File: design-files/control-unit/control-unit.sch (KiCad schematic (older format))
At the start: 126 parts, among them SW501 SW_Push, U501 74HCT04, U502 74HCT161, U503 AT28C64, U504 AT28C64, U505 74HCT273, U506 74HCT377, U507 4002, U508 74HCT32, U509 AT28C64, U510 74HCT08, U511 74HCT157, U512 AT28C64, U513 74HCT173, U514 74HCT173, U515 74HCT08

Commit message: control-unit: Add a .1 second RC delay on the reset button so that _RST is asserted momentarily at power-up.
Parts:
- added C?: 1µF, symbol Device:CP1_Small
- R501: value 1K -> 100K
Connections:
- net GND: now also C?.2
- net ~RST: now also C?.1
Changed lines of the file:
@@
 P 700 5200
 F 0 "R501" H 759 5246 50  0000 L CNN
-F 1 "1K" H 759 5155 50  0000 L CNN
+F 1 "100K" H 759 5155 50  0000 L CNN
 F 2 "Resistor_THT:R_Axial_DIN0204_L3.6mm_D1.6mm_P5.08mm_Horizontal" H 700 5200 50  0001 C CNN
 F 3 "~" H 700 5200 50  0001 C CNN
@@
 	700  5300 700  5400
 Wire Wire Line
-	950  5400 700  5400
+	950  5400 900  5400
 Connection ~ 700  5400
 Wire Wire Line
@@
 Connection ~ 10100 5450
 Connection ~ 9550 5450
+$Comp
+L Device:CP1_Small C?
+U 1 1 63D116B5
+P 900 5550
+F 0 "C?" H 991 5596 50  0000 L CNN
+F 1 "1µF" H 991 5505 50  0000 L CNN
+F 2 "" H 900 5550 50  0001 C CNN
+F 3 "~" H 900 5550 50  0001 C CNN
+	1    900  5550
+	1    0    0    -1
+$EndComp
+Connection ~ 900  5400
+Wire Wire Line
+	900  5400 700  5400
+$Comp
+L power:GND #PWR?
+U 1 1 63D1374A
+P 900 5650
+F 0 "#PWR?" H 900 5400 50  0001 C CNN
+F 1 "GND" H 905 5477 50  0000 C CNN
+F 2 "" H 900 5650 50  0001 C CNN
+F 3 "" H 900 5650 50  0001 C CNN
+	1    900  5650
+	1    0    0    -1
+$EndComp
+Wire Wire Line
+	900  5450 900  5400
 $EndSCHEMATC

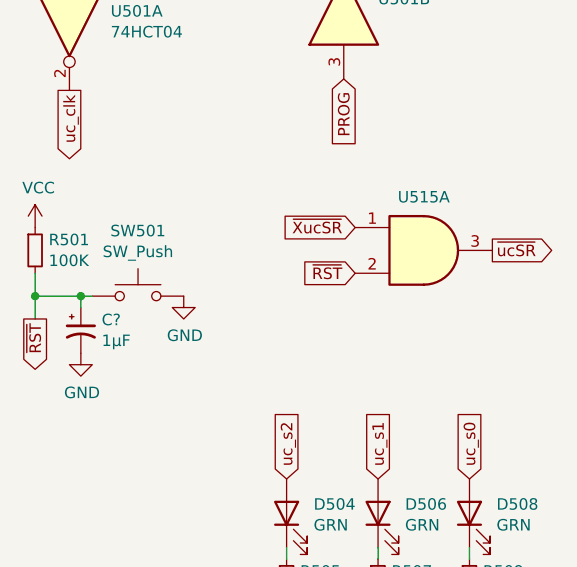
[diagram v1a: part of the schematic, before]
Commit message: control-unit: Discharge the capacitor on the reset signal through a 1K resistor.
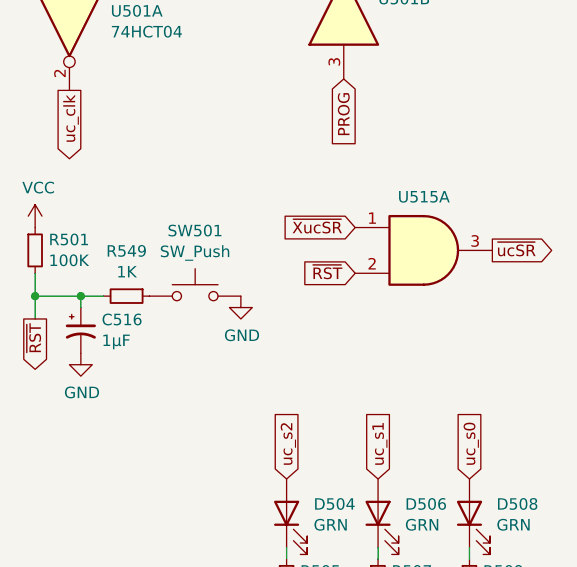
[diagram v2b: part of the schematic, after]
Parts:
- added R549: 1K, symbol Device:R_Small
- C516: renamed from C?; footprint (none) -> Capacitor_THT:CP_Radial_D6.3mm_P2.50mm; Mouser (none) -> 647-UVY2D010MED1TA
- R501: Mouser 594-SFR16S0001001JR5 -> 594-SFR16S0001003JA5
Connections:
- net ~RST: now also R549.2; no longer SW501.1
- new net: R549.1, SW501.1
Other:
- moved on the sheet: SW501
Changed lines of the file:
@@
 L Switch:SW_Push SW501
 U 1 1 630BB0DA
-P 1150 5400
-F 0 "SW501" H 1150 5685 50  0000 C CNN
-F 1 "SW_Push" H 1150 5594 50  0000 C CNN
-F 2 "Button_Switch_THT:SW_TH_Tactile_Omron_B3F-10xx" H 1150 5600 50  0001 C CNN
-F 3 "~" H 1150 5600 50  0001 C CNN
-F 4 "179-TS0266150BK100SC" H 1150 5400 50  0001 C CNN "Mouser"
-	1    1150 5400
+P 1400 5400
+F 0 "SW501" H 1400 5685 50  0000 C CNN
+F 1 "SW_Push" H 1400 5594 50  0000 C CNN
+F 2 "Button_Switch_THT:SW_TH_Tactile_Omron_B3F-10xx" H 1400 5600 50  0001 C CNN
+F 3 "~" H 1400 5600 50  0001 C CNN
+F 4 "179-TS0266150BK100SC" H 1400 5400 50  0001 C CNN "Mouser"
+	1    1400 5400
 	1    0    0    -1
 $EndComp
@@
 F 2 "Resistor_THT:R_Axial_DIN0204_L3.6mm_D1.6mm_P5.08mm_Horizontal" H 700 5200 50  0001 C CNN
 F 3 "~" H 700 5200 50  0001 C CNN
-F 4 "594-SFR16S0001001JR5" H 700 5200 50  0001 C CNN "Mouser"
+F 4 "594-SFR16S0001003JA5" H 700 5200 50  0001 C CNN "Mouser"
 	1    700  5200
 	1    0    0    -1
@@
 Wire Wire Line
 	700  5300 700  5400
-Wire Wire Line
-	950  5400 900  5400
 Connection ~ 700  5400
 Wire Wire Line
@@
 L power:GND #PWR0159
 U 1 1 6310BDAF
-P 1350 5400
-F 0 "#PWR0159" H 1350 5150 50  0001 C CNN
-F 1 "GND" H 1355 5227 50  0000 C CNN
-F 2 "" H 1350 5400 50  0001 C CNN
-F 3 "" H 1350 5400 50  0001 C CNN
-	1    1350 5400
+P 1600 5400
+F 0 "#PWR0159" H 1600 5150 50  0001 C CNN
+F 1 "GND" H 1605 5227 50  0000 C CNN
+F 2 "" H 1600 5400 50  0001 C CNN
+F 3 "" H 1600 5400 50  0001 C CNN
+	1    1600 5400
 	1    0    0    -1
 $EndComp
@@
 Connection ~ 9550 5450
 $Comp
-L Device:CP1_Small C?
+L Device:CP1_Small C516
 U 1 1 63D116B5
 P 900 5550
-F 0 "C?" H 991 5596 50  0000 L CNN
+F 0 "C516" H 991 5596 50  0000 L CNN
 F 1 "1µF" H 991 5505 50  0000 L CNN
-F 2 "" H 900 5550 50  0001 C CNN
+F 2 "Capacitor_THT:CP_Radial_D6.3mm_P2.50mm" H 900 5550 50  0001 C CNN
 F 3 "~" H 900 5550 50  0001 C CNN
+F 4 "647-UVY2D010MED1TA" H 900 5550 50  0001 C CNN "Mouser"
 	1    900  5550
 	1    0    0    -1
@@
 	900  5400 700  5400
 $Comp
-L power:GND #PWR?
+L power:GND #PWR0209
 U 1 1 63D1374A
 P 900 5650
-F 0 "#PWR?" H 900 5400 50  0001 C CNN
+F 0 "#PWR0209" H 900 5400 50  0001 C CNN
 F 1 "GND" H 905 5477 50  0000 C CNN
 F 2 "" H 900 5650 50  0001 C CNN
@@
 Wire Wire Line
 	900  5450 900  5400
+$Comp
+L Device:R_Small R549
+U 1 1 63D3F3F9
+P 1100 5400
+F 0 "R549" V 904 5400 50  0000 C CNN
+F 1 "1K" V 995 5400 50  0000 C CNN
+F 2 "" H 1100 5400 50  0001 C CNN
+F 3 "~" H 1100 5400 50  0001 C CNN
+F 4 "594-SFR16S0001001JR5" V 1100 5400 50  0001 C CNN "Mouser"
+	1    1100 5400
+	0    1    1    0
+$EndComp
+Wire Wire Line
+	900  5400 1000 5400
 $EndSCHEMATC

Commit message: Connect the insn latch, CC latch, and CC register to _RST.
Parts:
- R549: footprint (none) -> Resistor_THT:R_Axial_DIN0204_L3.6mm_D1.6mm_P5.08mm_Horizontal
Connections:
- net GND: no longer U513.15 (Mr)
- net VCC: no longer U505.1 (~Mr)
- net ~RST: now also U505.1 (~Mr)
- net cc_rst: now reaches U501.8, U514.15 (Mr)
- net cc_rst: now also U513.15 (Mr)
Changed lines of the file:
@@
 uc_clk
 $Comp
-L power:VCC #PWR0114
-U 1 1 6222178D
-P 5100 3750
-F 0 "#PWR0114" H 5100 3600 50  0001 C CNN
-F 1 "VCC" V 5115 3878 50  0000 L CNN
-F 2 "" H 5100 3750 50  0001 C CNN
-F 3 "" H 5100 3750 50  0001 C CNN
-	1    5100 3750
-	0    1    1    0
-$EndComp
-$Comp
 L power:GND #PWR0115
 U 1 1 62221D2F
@@
 $EndComp
 Connection ~ 9200 3950
-$Comp
-L power:GND #PWR0119
-U 1 1 629B2C28
-P 9200 4650
-F 0 "#PWR0119" H 9200 4400 50  0001 C CNN
-F 1 "GND" V 9205 4522 50  0000 R CNN
-F 2 "" H 9200 4650 50  0001 C CNN
-F 3 "" H 9200 4650 50  0001 C CNN
-	1    9200 4650
-	0    1    1    0
-$EndComp
 Text Notes 9650 4200 0    50   Italic 10
 CC\nLatch
@@
 F 0 "R549" V 904 5400 50  0000 C CNN
 F 1 "1K" V 995 5400 50  0000 C CNN
-F 2 "" H 1100 5400 50  0001 C CNN
+F 2 "Resistor_THT:R_Axial_DIN0204_L3.6mm_D1.6mm_P5.08mm_Horizontal" H 1100 5400 50  0001 C CNN
 F 3 "~" H 1100 5400 50  0001 C CNN
 F 4 "594-SFR16S0001001JR5" V 1100 5400 50  0001 C CNN "Mouser"
@@
 Wire Wire Line
 	900  5400 1000 5400
+Text GLabel 5100 3750 3    50   Input ~ 0
+~RST
+Text GLabel 15000 5200 3    50   Output ~ 0
+cc_rst
+Wire Wire Line
+	15000 5200 15000 4900
+Connection ~ 15000 4900
+Text GLabel 9200 4650 0    50   Input ~ 0
+cc_rst
 $EndSCHEMATC

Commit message: For ALU_B, don't use an AND gate with CLK to do the write-enable, as this could cause spurious rising-edges, and thus spurious loads into the register.  Use a pair of '157 muxes in front of the register intead. Change the ALB signal back to _ALB (active-low).
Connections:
- net GND: no longer R540.2
- net VCC: now also R540.2
- net at R540.1: now also D539.2 (A); no longer D539.1 (K)
- net ALB renamed ~ALB
- net ~ALB: now also D539.1 (K); no longer D539.2 (A)
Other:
- moved on the sheet: D539
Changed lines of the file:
@@
 ALS2
 Text GLabel 8850 900  1    50   Output ~ 0
-ALB
+~ALB
 Text GLabel 9000 900  1    50   Output ~ 0
 ~ALW
@@
 $EndComp
 $Comp
-L Device:LED D539
-U 1 1 6321D30E
-P 14550 7750
-F 0 "D539" V 14589 7632 50  0000 R CNN
-F 1 "GRN" V 14498 7632 50  0000 R CNN
-F 2 "LED_THT:LED_D5.0mm" H 14550 7750 50  0001 C CNN
-F 3 "~" H 14550 7750 50  0001 C CNN
-	1    14550 7750
-	0    -1   -1   0
-$EndComp
-$Comp
 L Device:R_Small R540
 U 1 1 6321D314
@@
 $EndComp
 $Comp
-L power:GND #PWR0176
-U 1 1 6321D32C
-P 14550 8150
-F 0 "#PWR0176" H 14550 7900 50  0001 C CNN
-F 1 "GND" H 14555 7977 50  0000 C CNN
-F 2 "" H 14550 8150 50  0001 C CNN
-F 3 "" H 14550 8150 50  0001 C CNN
-	1    14550 8150
-	1    0    0    -1
-$EndComp
-$Comp
 L power:GND #PWR0177
 U 1 1 6321D33E
@@
 ~ALW
 Text GLabel 14550 7600 1    50   Input ~ 0
-ALB
+~ALB
 $Comp
 L Device:LED D524
@@
 Text GLabel 9200 4650 0    50   Input ~ 0
 cc_rst
+$Comp
+L power:VCC #PWR?
+U 1 1 623040CC
+P 14550 8150
+F 0 "#PWR?" H 14550 8000 50  0001 C CNN
+F 1 "VCC" H 14565 8323 50  0000 C CNN
+F 2 "" H 14550 8150 50  0001 C CNN
+F 3 "" H 14550 8150 50  0001 C CNN
+	1    14550 8150
+	-1   0    0    1
+$EndComp
+$Comp
+L Device:LED D539
+U 1 1 6321D30E
+P 14550 7750
+F 0 "D539" V 14500 7650 50  0000 R CNN
+F 1 "GRN" V 14600 7650 50  0000 R CNN
+F 2 "LED_THT:LED_D5.0mm" H 14550 7750 50  0001 C CNN
+F 3 "~" H 14550 7750 50  0001 C CNN
+	1    14550 7750
+	0    -1   1    0
+$EndComp
 $EndSCHEMATC

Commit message: Rework to use DIP register packs for the LEDs.
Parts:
- removed R502, R503, R504, R505, R506, R507, R508, R509, R510, R511, R512, R513, R514, R515, R516, R517, R518, R519, R520, R521, R522, R523, R524, R525, R526, R527, R528, R529, R530, R531, R532, R533, R534, R535, R536, R537, R538, R539, R540, R541, R542, R543, R544, R545, R546, R547, R548: 330, Resistor_THT:R_Axial_DIN0204_L3.6mm_D1.6mm_P5.08mm_Horizontal, symbol Device:R_Small
- added D548: YEL, LED_THT:LED_D5.0mm, symbol Device:LED
- added RN501: 330x8, Package_DIP:DIP-16_W7.62mm_Socket, symbol Device:R_Pack08_Split
- added RN502, RN503, RN504, RN505, RN506: 330 x 8, Package_DIP:DIP-16_W7.62mm_Socket, symbol Device:R_Pack08
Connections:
- net GND: now also RN501.1 (R1.1), RN501.2 (R2.1), RN501.3 (R3.1), RN501.4 (R4.1), RN501.5 (R5.1), RN501.6 (R6.1), RN501.7 (R7.1), RN501.8 (R8.1), RN502.3 (R3.1), RN502.4 (R4.1), RN502.5 (R5.1), RN503.2 (R2.1), RN503.4 (R4.1), RN505.1 (R1.1), RN505.2 (R2.1), RN505.3 (R3.1), RN505.4 (R4.1), RN505.5 (R5.1), RN505.6 (R6.1), RN505.7 (R7.1), RN505.8 (R8.1), RN506.1 (R1.1), RN506.5 (R5.1), RN506.6 (R6.1), RN506.7 (R7.1), RN506.8 (R8.1)
- net VCC: now also RN502.1 (R1.1), RN502.2 (R2.1), RN502.6 (R6.1), RN502.7 (R7.1), RN502.8 (R8.1), RN503.1 (R1.1), RN503.3 (R3.1), RN503.5 (R5.1), RN503.6 (R6.1), RN503.7 (R7.1), RN503.8 (R8.1), RN504.1 (R1.1), RN504.2 (R2.1), RN504.3 (R3.1), RN504.4 (R4.1), RN504.5 (R5.1), RN504.6 (R6.1), RN504.7 (R7.1), RN504.8 (R8.1), RN506.2 (R2.1), RN506.3 (R3.1), RN506.4 (R4.1)
- net uc_clk: now also D548.2 (A)
- net at D540.1 (K): now also RN501.12 (R5.2)
- net at D542.1 (K): now also RN501.11 (R6.2)
- net at D544.1 (K): now also RN501.10 (R7.2)
- net at D546.1 (K): now also RN501.9 (R8.2)
- net at D532.1 (K): now also RN505.12 (R5.2)
- net at D533.1 (K): now also RN505.11 (R6.2)
- net at D535.1 (K): now also RN505.10 (R7.2)
- net at D537.1 (K): now also RN505.9 (R8.2)
- net at D525.1 (K): now also RN505.16 (R1.2)
- net at D527.1 (K): now also RN505.15 (R2.2)
- net at D529.1 (K): now also RN505.14 (R3.2)
- net at D531.1 (K): now also RN505.13 (R4.2)
- net at D541.1 (K): now also RN506.12 (R5.2)
- net at D543.1 (K): now also RN506.11 (R6.2)
- net at D545.1 (K): now also RN506.10 (R7.2)
- net at D547.1 (K): now also RN506.9 (R8.2)
- net at D534.1 (K): now also RN506.16 (R1.2)
- net at D536.2 (A): now also RN506.15 (R2.2)
- net at D538.2 (A): now also RN506.14 (R3.2)
- net at D539.2 (A): now also RN506.13 (R4.2)
- net at D524.2 (A): now also RN504.12 (R5.2)
- net at D526.2 (A): now also RN504.11 (R6.2)
- net at D528.2 (A): now also RN504.10 (R7.2)
- net at D530.2 (A): now also RN504.9 (R8.2)
- net at D520.2 (A): now also RN504.16 (R1.2)
- net at D521.2 (A): now also RN504.15 (R2.2)
- net at D522.2 (A): now also RN504.14 (R3.2)
- net at D523.2 (A): now also RN504.13 (R4.2)
- net at D516.2 (A): now also RN503.12 (R5.2)
- net at D517.2 (A): now also RN503.11 (R6.2)
- net at D518.2 (A): now also RN503.10 (R7.2)
- net at D519.2 (A): now also RN503.9 (R8.2)
- net at D512.2 (A): now also RN503.16 (R1.2)
- net at D513.1 (K): now also RN503.15 (R2.2)
- net at D514.2 (A): now also RN503.14 (R3.2)
- net at D515.1 (K): now also RN503.13 (R4.2)
- net at D507.1 (K): now also RN502.12 (R5.2)
- net at D509.2 (A): now also RN502.11 (R6.2)
- net at D510.2 (A): now also RN502.10 (R7.2)
- net at D511.2 (A): now also RN502.9 (R8.2)
- net at D501.2 (A): now also RN502.16 (R1.2)
- net at D502.2 (A): now also RN502.15 (R2.2)
- net at D503.1 (K): now also RN502.14 (R3.2)
- net at D505.1 (K): now also RN502.13 (R4.2)
- net at D504.1 (K): now also RN501.16 (R1.2)
- net at D506.1 (K): now also RN501.15 (R2.2)
- net at D508.1 (K): now also RN501.14 (R3.2)
- new net: D548.1 (K), RN501.13 (R4.2)
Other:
- moved on the sheet: D504, D506, D508

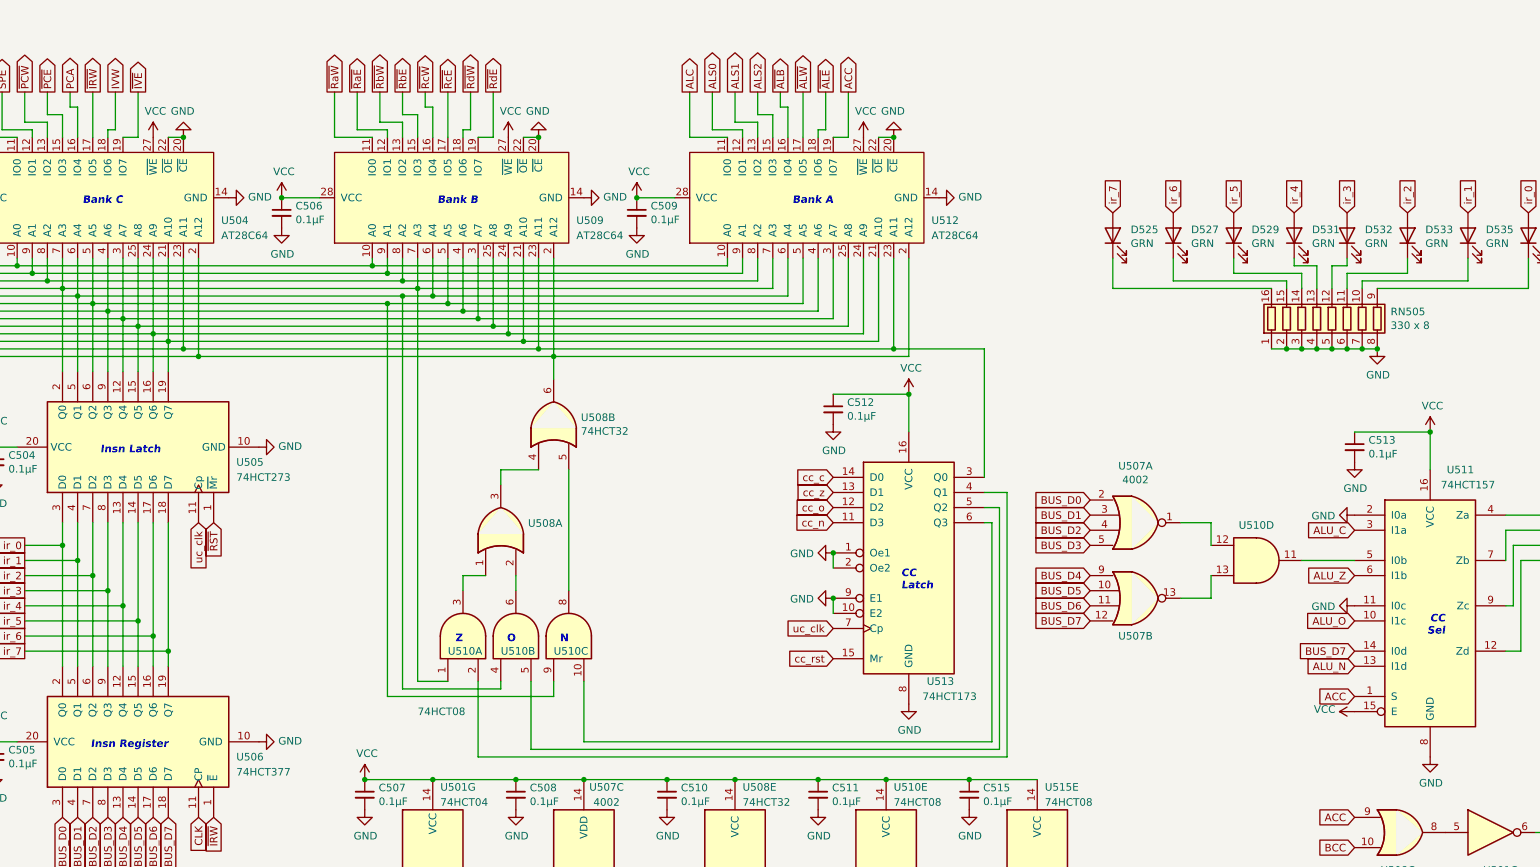
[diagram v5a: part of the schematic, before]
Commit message: Make the IV register a '377; there isn't really any reason to make it reset to 0 at the beginning of each instruction.
While here, fix the CC selector; Enable is active-low.
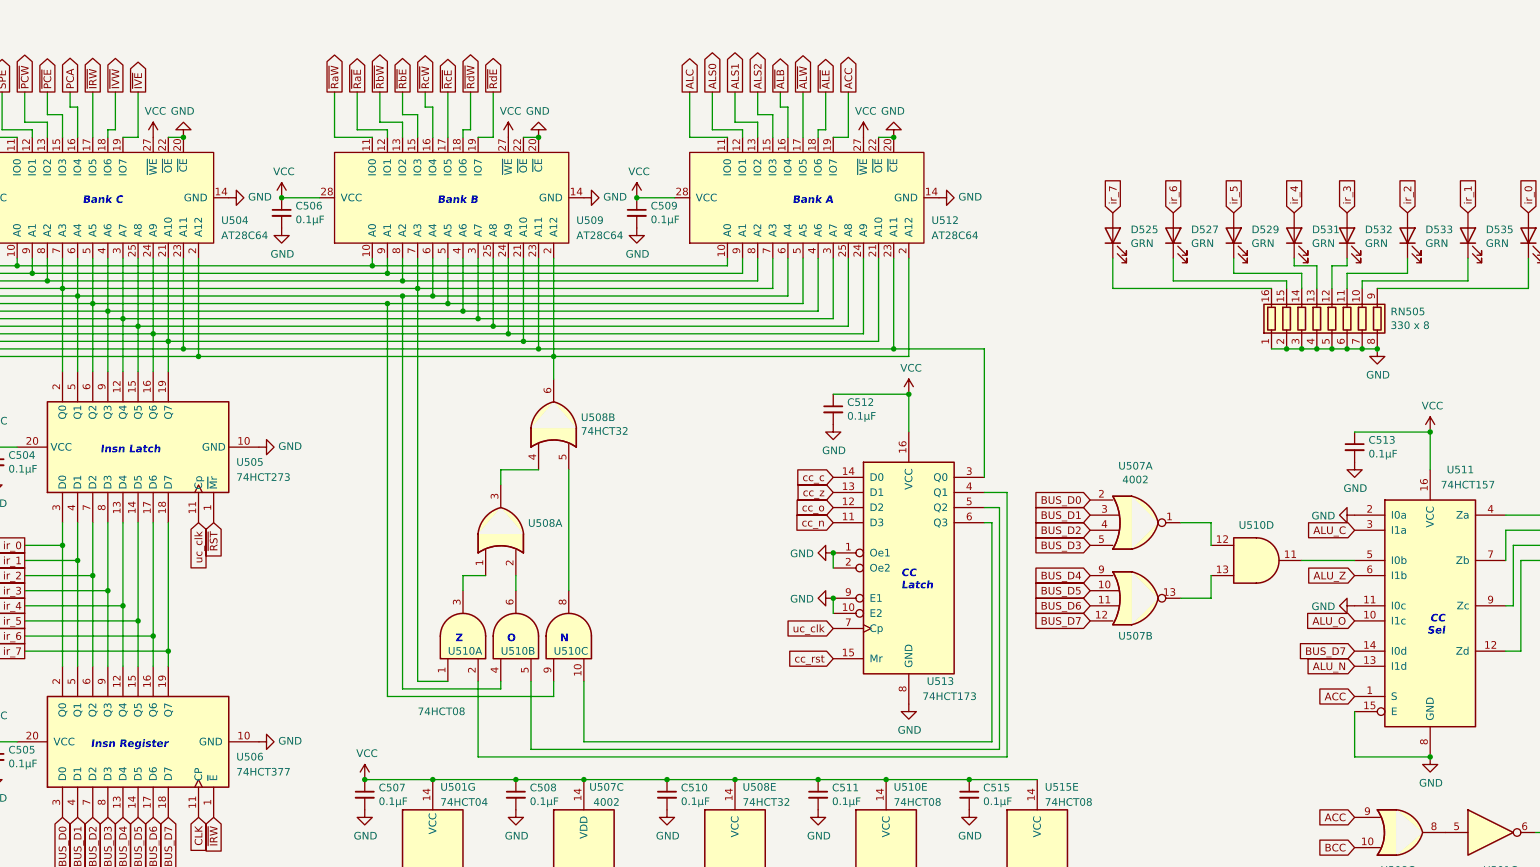
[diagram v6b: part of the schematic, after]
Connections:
- net GND: now also U511.15 (E)
- net IVW: no longer U504.18 (IO6)
- net VCC: no longer U511.15 (E)
- new net ~IVW: U504.18 (IO6)
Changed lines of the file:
@@
 ~IRW
 Text GLabel 4450 900  1    50   Output ~ 0
-IVW
+~IVW
 Text GLabel 4600 900  1    50   Output ~ 0
 ~IVE
@@
 ALU_N
 $Comp
-L power:VCC #PWR0126
-U 1 1 62BC1922
-P 12650 5000
-F 0 "#PWR0126" H 12650 4850 50  0001 C CNN
-F 1 "VCC" V 12665 5127 50  0000 L CNN
-F 2 "" H 12650 5000 50  0001 C CNN
-F 3 "" H 12650 5000 50  0001 C CNN
-	1    12650 5000
-	0    -1   -1   0
-$EndComp
-$Comp
 L power:GND #PWR0127
 U 1 1 62BC2254
@@
 	1    0    0    -1
 $EndComp
+Wire Wire Line
+	12650 5000 12650 5300
+Wire Wire Line
+	12650 5300 13150 5300
+Connection ~ 13150 5300
 $EndSCHEMATC
